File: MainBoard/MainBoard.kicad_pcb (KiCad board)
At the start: 2 copper layers, 27 parts, among them J1 Conn_01x20, J10 Conn_01x04, J11-L-FRONT1 Screw_Terminal_01x02, J12-L-REAR1 Screw_Terminal_01x02, J13-R-FRONT1 Screw_Terminal_01x02, J14-R-REAR1 Screw_Terminal_01x02, J2 Conn_01x12, J3 Conn_01x10, J4 Conn_01x07, J9 Conn_01x04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

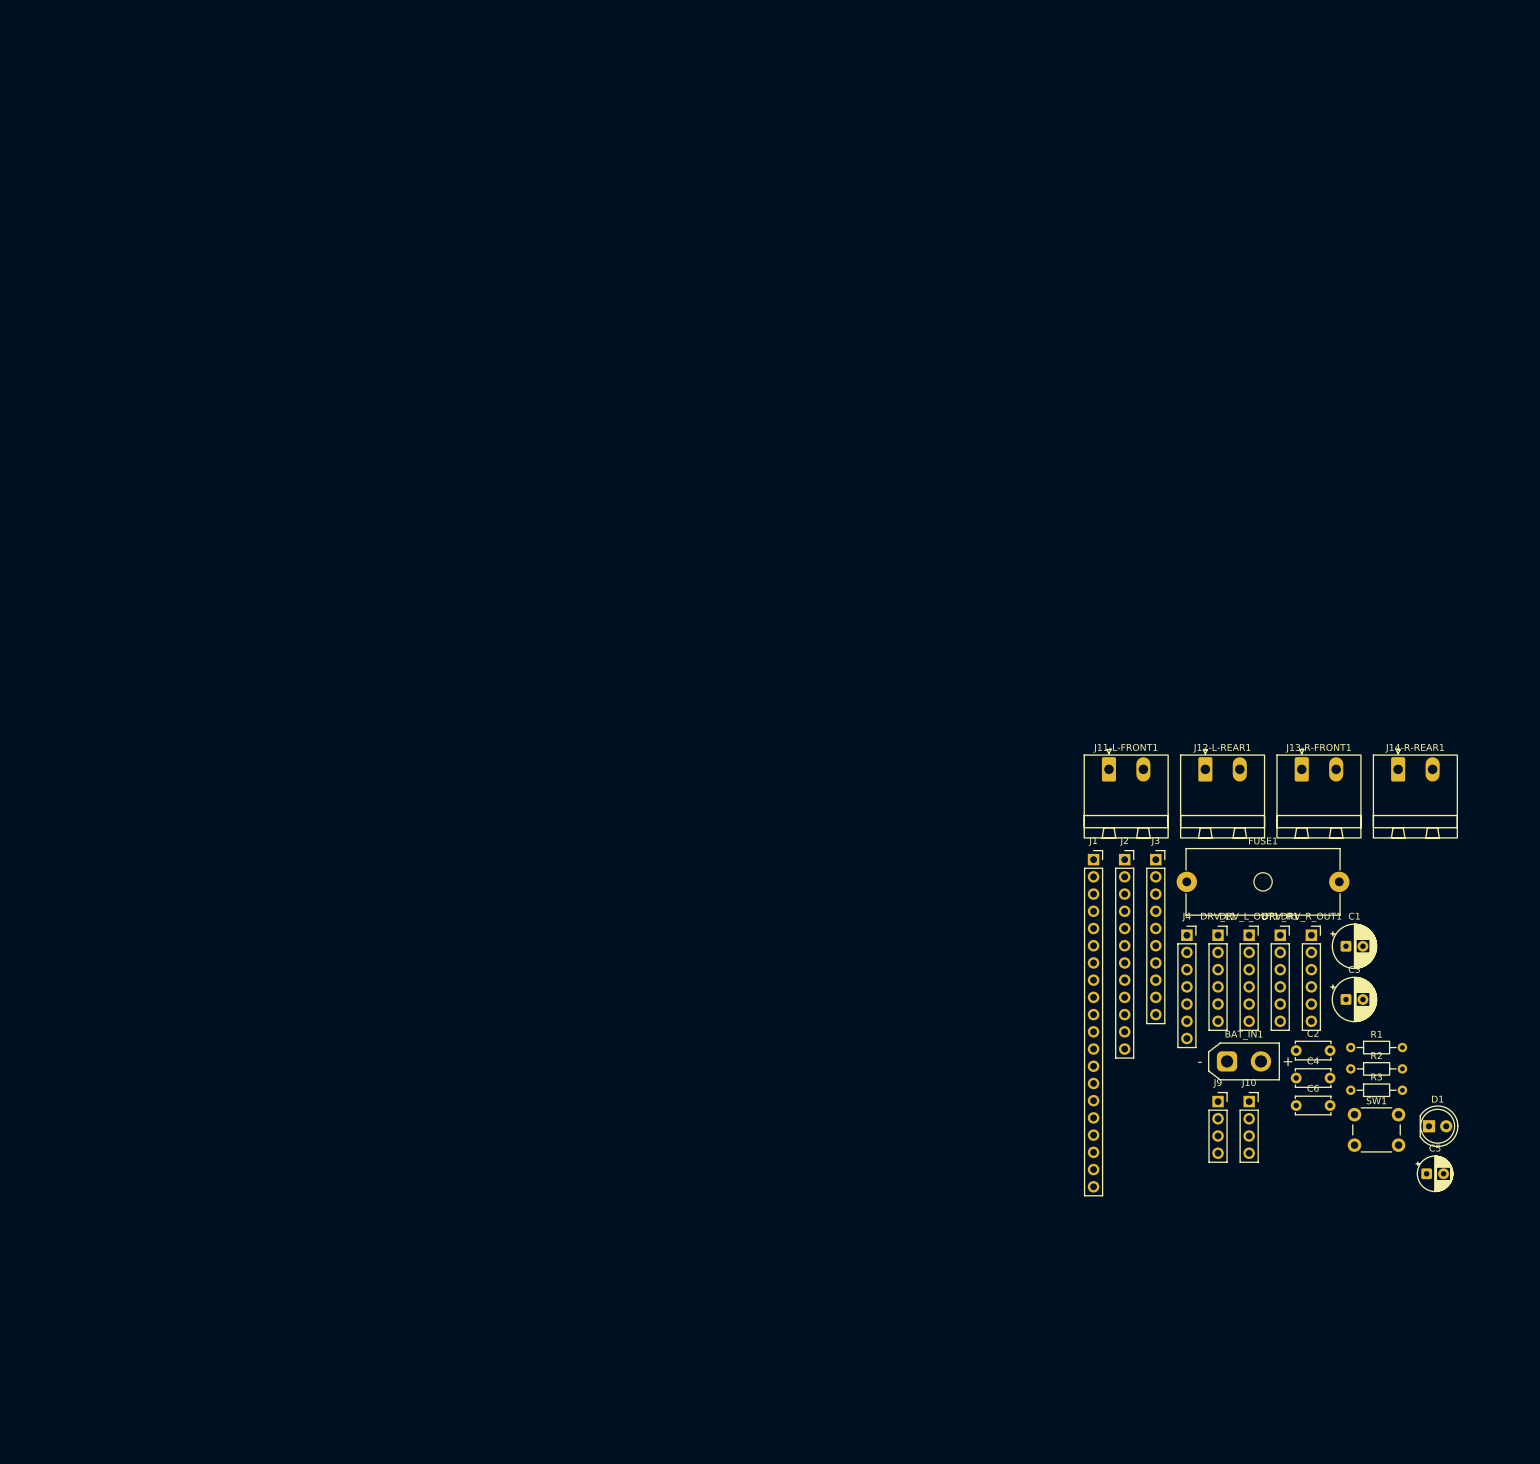
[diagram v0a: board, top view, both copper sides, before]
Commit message: mini360_mp1584en회로수정
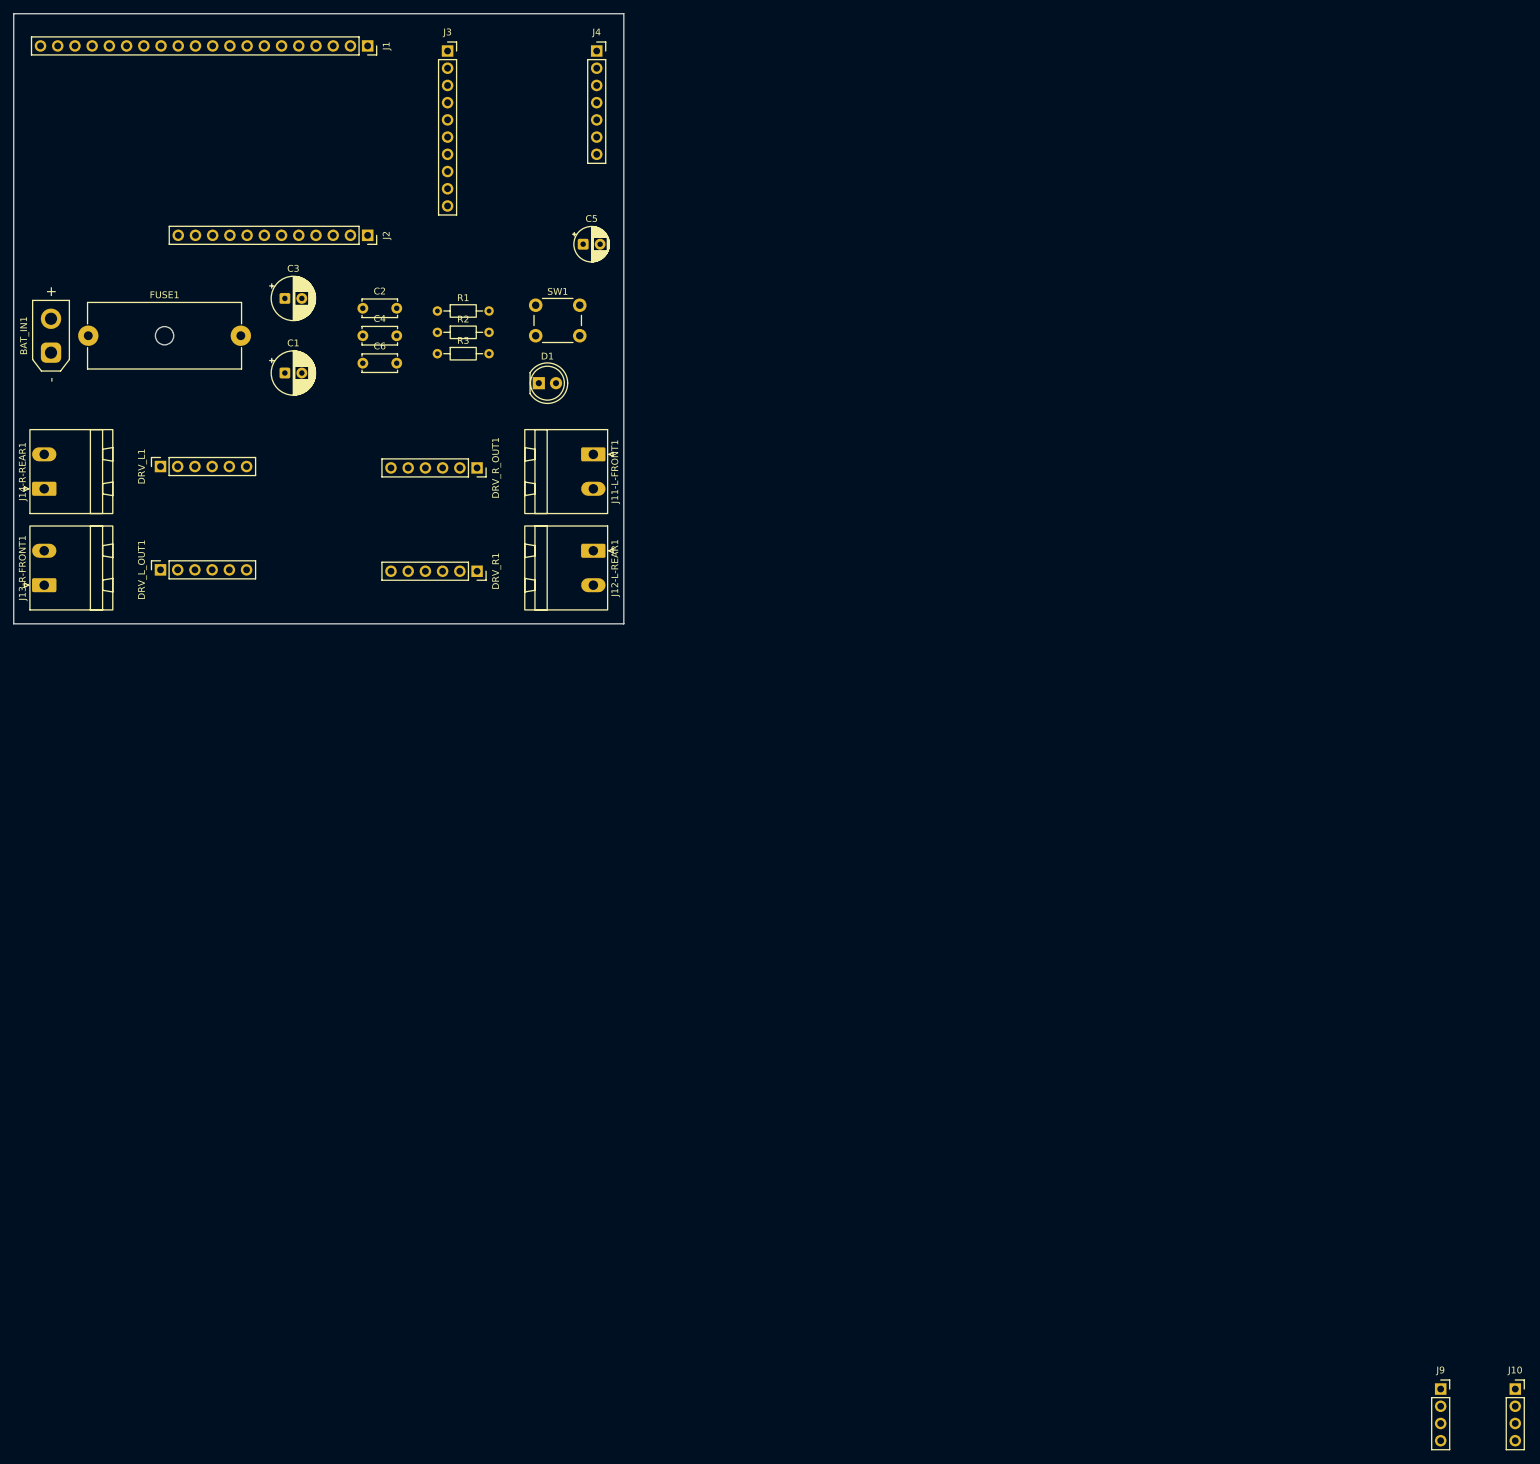
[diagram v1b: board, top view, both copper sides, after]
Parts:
- moved J14-R-REAR1 204.0 mm to (-40.5, 25.1), turned to 90 degrees
- moved BAT_IN1 202.6 mm to (-39.5, 5.00), turned to 90 degrees
- moved C3 187.6 mm to (-5.00, -3.00)
- moved J13-R-FRONT1 187.5 mm to (-40.5, 39.3), turned to 90 degrees
- moved C5 185.2 mm to (39.0, -11.0)
- moved FUSE1 181.0 mm to (-34.0, 2.50)
- moved C1 177.9 mm to (-5.00, 8.00)
- moved C2 175.9 mm to (6.50, -1.55)
- moved C4 175.9 mm to (6.50, 2.50)
- moved C6 175.9 mm to (6.50, 6.55)
- moved R1 173.1 mm to (17.5, -1.15)
- moved R2 173.1 mm to (17.5, 2.00)
- moved R3 173.1 mm to (17.5, 5.15)
- moved D1 171.1 mm to (32.5, 9.50)
- moved DRV_L1 170.6 mm to (-23.4, 21.8), turned to 90 degrees
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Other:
- board outline added: 90 x 90 mm

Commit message: 전원배선완료
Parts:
- removed J9: Conn_01x04, Connector_PinSocket_2.54mm:PinSocket_1x04_P2.54mm_Vertical
- added C7: 100nF, Capacitor_THT:C_Disc_D5.0mm_W2.5mm_P5.00mm, F.Cu at (121.9, 119.4)
- added C8: 100nF, Capacitor_THT:C_Disc_D5.0mm_W2.5mm_P5.00mm, F.Cu at (87.6, 62.2)
- added C9: 100nF, Capacitor_THT:C_Disc_D5.0mm_W2.5mm_P5.00mm, F.Cu at (58.4, 55.9)
- added MINI360_OUT1: Conn_01x04, Connector_PinSocket_2.54mm:PinSocket_1x04_P2.54mm_Vertical, F.Cu at (130.8, 55.9)
- added MP1584EN_IN1: Conn_01x06, Connector_PinSocket_2.54mm:PinSocket_1x06_P2.54mm_Vertical, F.Cu at (111.8, 40.6)
- added MP1584EN_OUT1: Conn_01x06, Connector_PinSocket_2.54mm:PinSocket_1x06_P2.54mm_Vertical, F.Cu at (111.8, 61.0)
- C1: value 100uF -> 470uF
- moved J14-R-REAR1 199.2 mm to (137.3, 115.0), turned to -90 degrees
- moved J13-R-FRONT1 188.1 mm to (137.3, 100.7), turned to -90 degrees
- moved J1 176.9 mm to (120.6, 95.6)
- moved J2 176.9 mm to (120.6, 123.5)
- moved C6 139.0 mm to (132.2, 66.0)
- moved C3 137.0 mm to (111.8, 68.6)
- moved R1 135.0 mm to (108.0, 99.1), turned to -90 degrees
- moved SW1 134.2 mm to (130.7, 88.9)
- moved DRV_R_OUT1 128.4 mm to (135.9, 83.8), turned to 180 degrees
- moved R2 127.6 mm to (100.3, 99.1), turned to -90 degrees
- moved J3 127.5 mm to (89.7, 66.6)
- moved C4 126.8 mm to (110.5, 74.9)
- moved MINI360_IN1 125.8 mm to (130.8, 40.6), turned to 90 degrees
- moved C5 118.7 mm to (133.4, 61.0)
- moved DRV_L1 115.7 mm to (81.3, 71.1), turned to 0 degrees
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- renumbered J10 to MINI360_IN1
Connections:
- MINI360_IN1 pad 2: GND -> /VBAT_F
- MINI360_IN1 pad 3: VCC -> GND
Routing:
- net /VBAT_F: track 0.00 -> 132.7 mm
- net VCC: track 0.00 -> 102.1 mm, vias 0 -> 4
- net /5V0: track 0.00 -> 69.4 mm
- net GND: track 0.00 -> 50.5 mm
- net /VBAT: track 0.00 -> 8.21 mm
- net Net-(D1-K): track 0.00 -> 5.39 mm

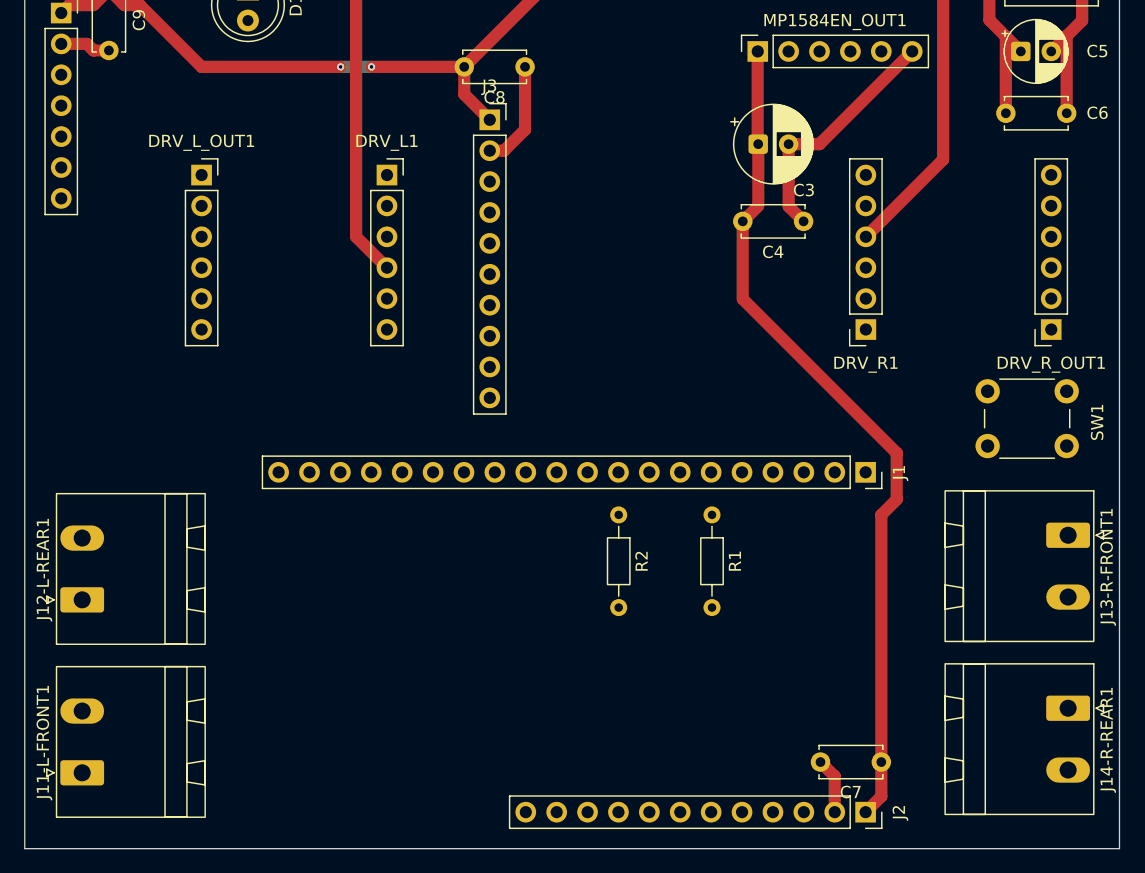
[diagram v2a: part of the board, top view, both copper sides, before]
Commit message: drv8833_R배선필요
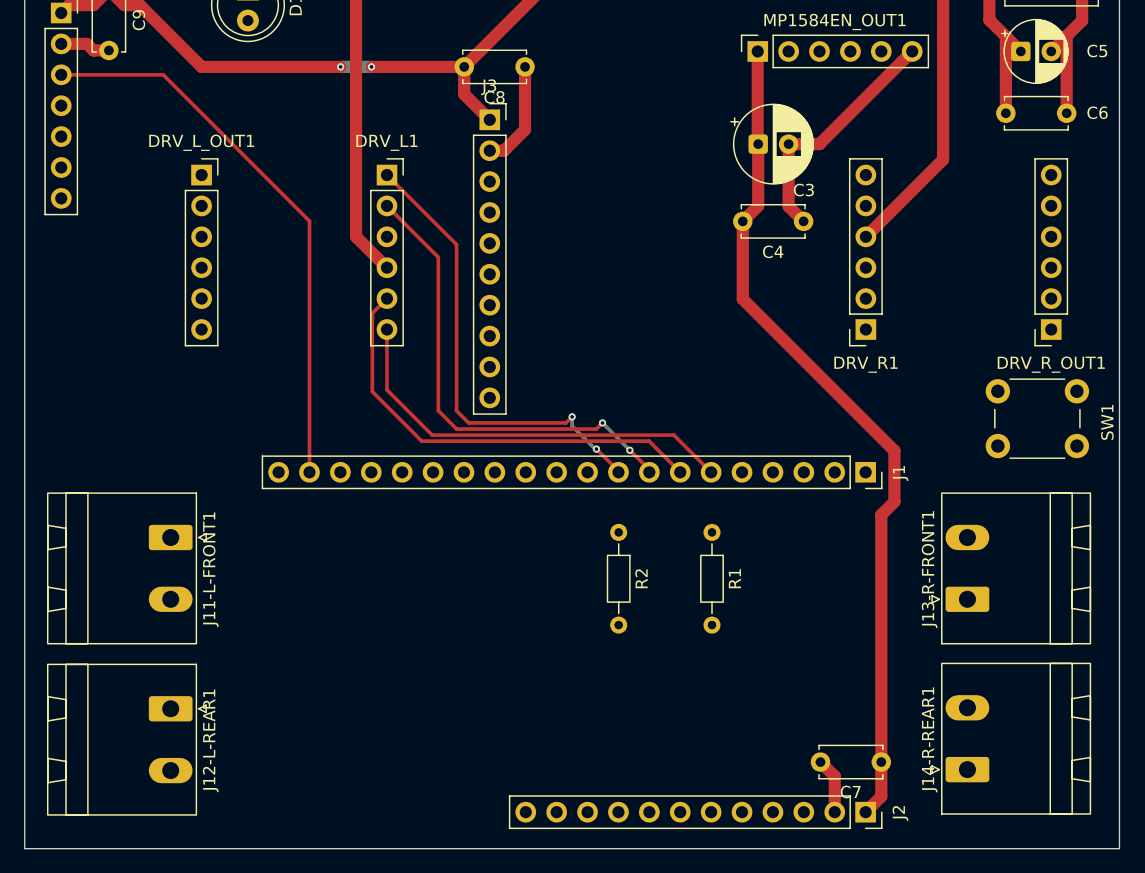
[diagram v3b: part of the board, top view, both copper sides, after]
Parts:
- moved J11-L-FRONT1 20.7 mm to (63.5, 100.9), turned to -90 degrees
- moved J12-L-REAR1 11.5 mm to (63.5, 115.0), turned to -90 degrees
- moved J13-R-FRONT1 9.81 mm to (129.0, 106.0), turned to 90 degrees
- moved J14-R-REAR1 9.69 mm to (129.0, 120.0), turned to 90 degrees
- moved R1 1.44 mm to (108.0, 100.5)
- moved R2 1.44 mm to (100.3, 100.5)
- moved SW1 0.84 mm to (131.5, 88.9)
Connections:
- J4 pad 3: /IO16 -> /IO36
- J4 pad 4: /IO17 -> /T1
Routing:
- net /IO36: track 0.00 -> 46.0 mm
- net /IO14: track 0.00 -> 38.8 mm, vias 0 -> 2
- net /IO15: track 0.00 -> 38.1 mm, vias 0 -> 2
- net /IO13: track 0.00 -> 36.2 mm
- net /IO12: track 0.00 -> 34.4 mm

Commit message: PCB상 핀 배치가 짧고 편한 라우팅을 위해 핀맵 재설정 필요
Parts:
- moved SW1 76.5 mm to (55.0, 88.9)
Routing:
- net /IO12: track 34.4 -> 39.4 mm
- net /IO15: track 38.1 -> 43.0 mm
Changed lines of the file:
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@@
 	(footprint "Button_Switch_THT:SW_PUSH_6mm"
 		(layer "F.Cu")
-		(at 131.5 88.9)
+		(at 55 88.9)
 		(descr "Generic 6mm SW tactile push button")
 		(tags "tact sw push 6mm")
@@
 	)
 	(segment
+		(start 100.31 95.56)
+		(end 100.31 100.48)
+		(width 0.3)
+		(layer "F.Cu")
+		(net "/IO15")
+	)
+	(segment
+		(start 100.31 100.48)
+		(end 100.33 100.5)
+		(width 0.3)
+		(layer "F.Cu")
+		(net "/IO15")
+	)
+	(segment
 		(start 87 76.839999)
 		(end 81.280001 71.12)
@@
 	)
 	(segment
+		(start 107.93 100.43)
+		(end 108 100.5)
+		(width 0.3)
+		(layer "F.Cu")
+		(net "/IO12")
+	)
+	(segment
 		(start 85 92.5)
 		(end 104.87 92.5)
@@
 		(width 0.3)
 		(layer "F.Cu")
+		(net "/IO12")
+	)
+	(segment
+		(start 107.93 95.56)
+		(end 107.93 100.43)
+		(width 0.3)
+		(layer "F.Cu")

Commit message: 배선 삭제, 재배치 필요. 핀 넘버 정리
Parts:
- moved J3 2.30 mm to (92.0, 66.2)
- moved C7 0.38 mm to (121.9, 119.0)
- moved C8 0.26 mm to (87.5, 62.0)
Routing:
- net /VBAT_F: track 132.7 -> 1.34 mm
- net VCC: track 102.1 -> 0.92 mm, vias 4 -> 0
- net /5V0: track 69.2 -> 0.06 mm
- net GND: track 50.5 -> 0.00 mm
- net /IO36: track 46.0 -> 0.00 mm
- net /IO15: track 43.0 -> 0.13 mm, vias 2 -> 0
- net /IO12: track 39.4 -> 0.10 mm
- net /IO14: track 38.8 -> 0.42 mm, vias 2 -> 0
- net /IO13: track 36.2 -> 0.00 mm
- net /VBAT: track 8.21 -> 0.00 mm
- net Net-(D1-K): track 5.39 -> 0.00 mm
